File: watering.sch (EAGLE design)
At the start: 36 parts, among them IC1 LM324N, IC2 7805T, J1 DCJ0202, Q1 IRF510, T1 2N2222, T2 2N2222, T3 2N2222A

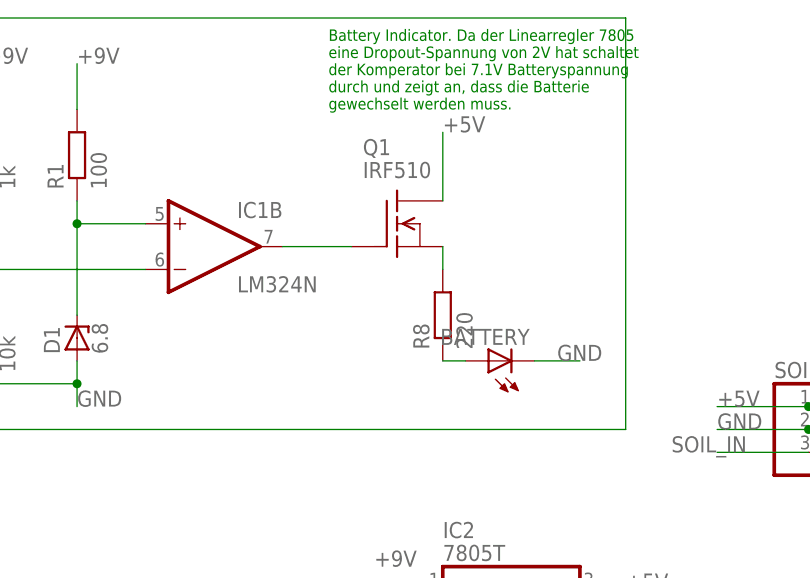
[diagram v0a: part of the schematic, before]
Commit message: Add pull-down resistor for MOSFET and changed MOSFET type to IRLZ44N
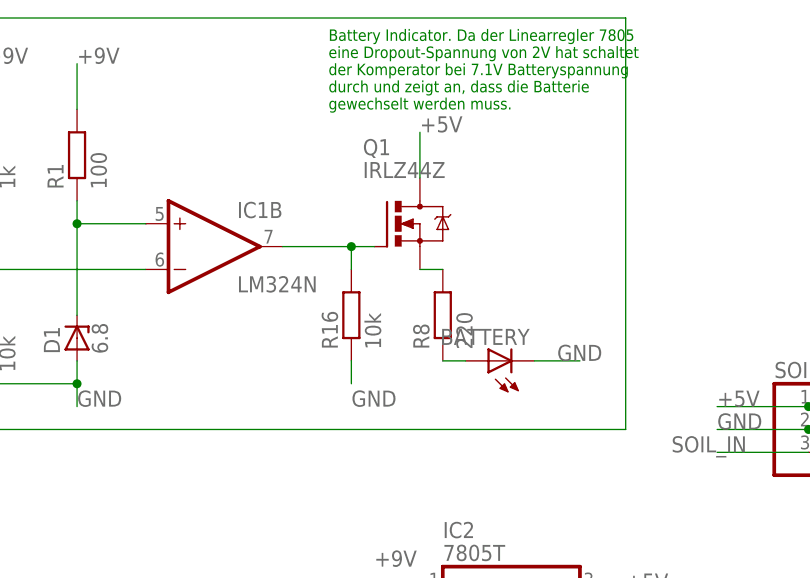
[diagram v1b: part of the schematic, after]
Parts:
- added R16: 10k, resistor:R-EU_0204/5
- Q1: value IRF510 -> IRLZ44Z; device transistor-fet:IRF510 -> transistor-power:IRLZ44Z
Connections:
- net GND: now also R16.1
- net N$7: now also R16.2
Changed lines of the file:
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@@
 <part name="R6" library="resistor" deviceset="R-EU_" device="0204/5" value="1k"/>
 <part name="R7" library="resistor" deviceset="R-EU_" device="0204/5" value="10k"/>
-<part name="Q1" library="transistor-fet" deviceset="IRF510" device=""/>
+<part name="Q1" library="transistor-power" deviceset="IRLZ44Z" device=""/>
 <part name="R8" library="resistor" deviceset="R-EU_" device="0204/5" value="220"/>
 <part name="BATTERY" library="led" deviceset="LED" device="3MM"/>
@@
 <part name="JP1" library="pinhead" deviceset="PINHD-1X1" device="" value="JP2_DSIG"/>
 <part name="R15" library="resistor" deviceset="R-EU_" device="0204/5" value="4.7k"/>
+<part name="R16" library="resistor" deviceset="R-EU_" device="0204/5" value="10k"/>
 </parts>
 <sheets>
@@
 </instance>
 <instance part="R15" gate="G$1" x="-38.1" y="-30.48" rot="R180"/>
+<instance part="R16" gate="G$1" x="-78.74" y="101.6" rot="R90"/>
 </instances>
 <busses>
@@
 <wire x1="-33.02" y1="-30.48" x2="-27.94" y2="-30.48" width="0.1524" layer="91"/>
 <label x="-30.48" y="-30.48" size="1.27" layer="95"/>
+</segment>
+<segment>
+<pinref part="R16" gate="G$1" pin="1"/>
+<wire x1="-78.74" y1="96.52" x2="-78.74" y2="93.98" width="0.1524" layer="91"/>
+<label x="-78.74" y="91.44" size="1.778" layer="95"/>
 </segment>
 </net>
@@
 <segment>
 <pinref part="Q1" gate="G$1" pin="D"/>
-<wire x1="-68.58" y1="114.3" x2="-68.58" y2="121.92" width="0.1524" layer="91"/>
-<label x="-68.58" y="121.92" size="1.778" layer="95"/>
+<wire x1="-71.12" y1="116.84" x2="-71.12" y2="121.92" width="0.1524" layer="91"/>
+<label x="-71.12" y="121.92" size="1.778" layer="95"/>
 </segment>
 <segment>
@@
 <pinref part="Q1" gate="G$1" pin="G"/>
 <wire x1="-86.36" y1="109.22" x2="-78.74" y2="109.22" width="0.1524" layer="91"/>
+<pinref part="R16" gate="G$1" pin="2"/>
+<wire x1="-78.74" y1="109.22" x2="-76.2" y2="109.22" width="0.1524" layer="91"/>
+<wire x1="-78.74" y1="106.68" x2="-78.74" y2="109.22" width="0.1524" layer="91"/>
+<junction x="-78.74" y="109.22"/>
 </segment>
 </net>
@@
 <pinref part="Q1" gate="G$1" pin="S"/>
 <pinref part="R8" gate="G$1" pin="2"/>
-<wire x1="-68.58" y1="109.22" x2="-68.58" y2="106.68" width="0.1524" layer="91"/>
-</segment>
-</net>
+<wire x1="-71.12" y1="106.68" x2="-68.58" y2="106.68" width="0.1524" layer="91"/>
+</segment>
+</net>

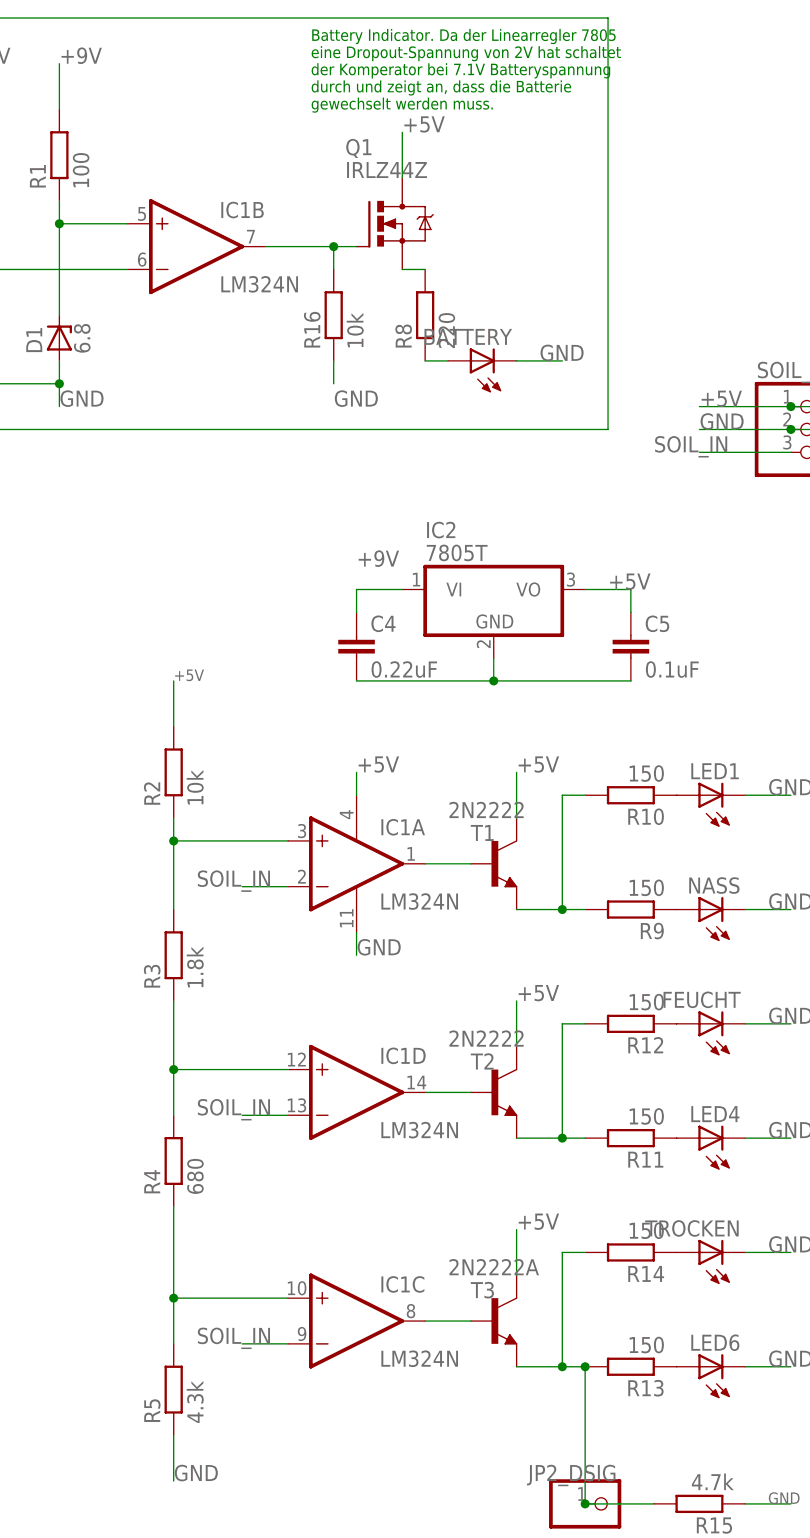
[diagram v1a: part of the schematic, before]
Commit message: Create watering indicator v2.0 for SMD
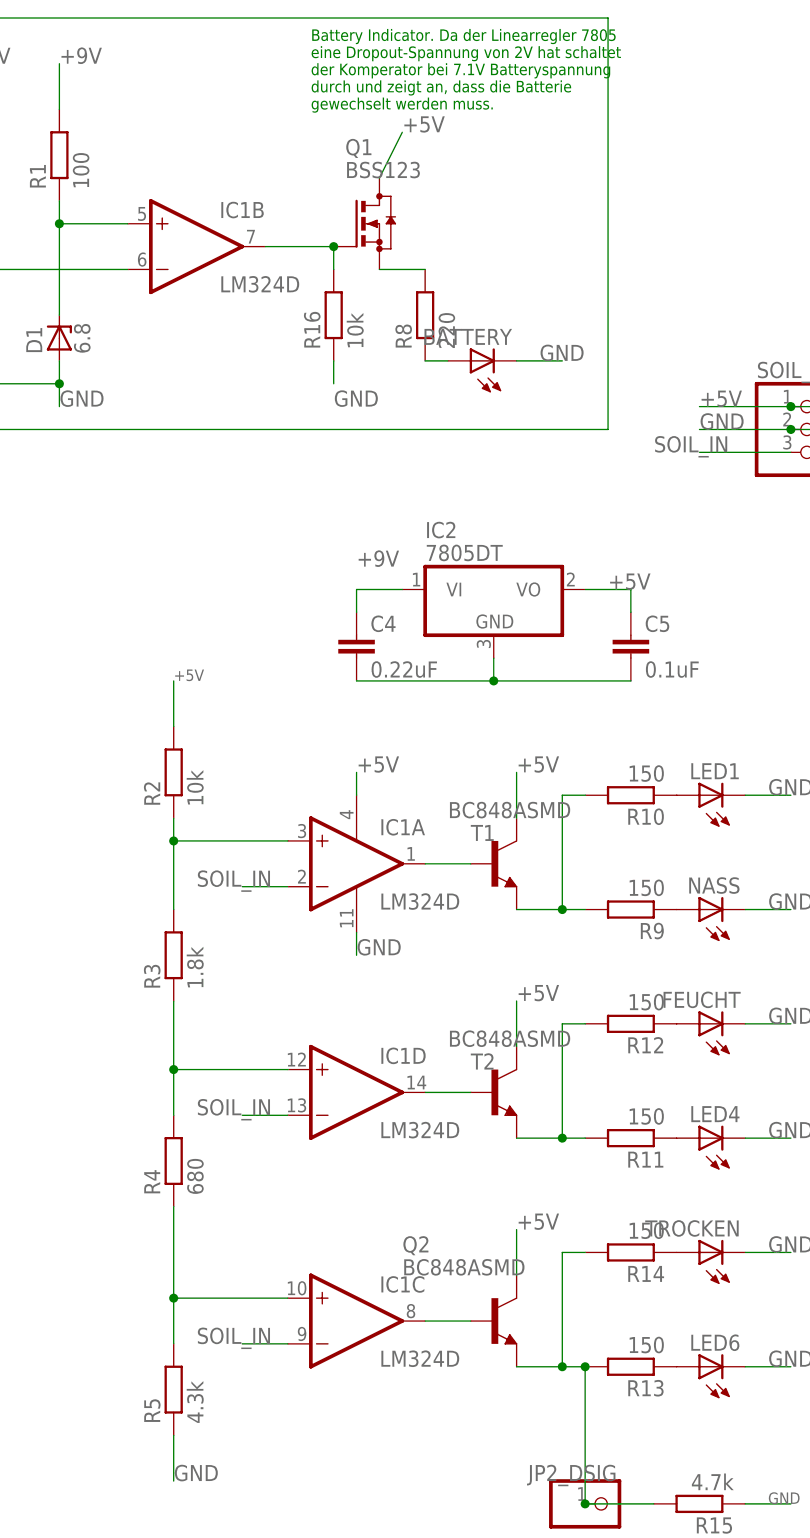
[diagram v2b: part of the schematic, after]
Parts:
- removed T3: 2N2222A, transistor-npn:2N2222A
- added Q2: BC848ASMD, transistor-npn:BC848ASMD
- BATTERY, FEUCHT, LED1, LED4, LED6, NASS, TROCKEN: device led:LED3MM -> led:LEDSML0805
- C2, C3, C4, C5: device rcl:C-EU025-025X050 -> rcl:C-EUC0805
- D1: device diode:ZENER-DIODEZD-7.5 -> diode:ZENER-DIODESOD80C
- IC1: value LM324N -> LM324D; device linear:LM324N -> linear:LM324D
- IC2: value 7805T -> 7805DT; device linear:7805T -> linear:7805DT
- Q1: value IRLZ44Z -> BSS123; device transistor-power:IRLZ44Z -> transistor-small-signal:BSS123
- R1, R10, R11, R12, R13, R14, R15, R16, R2, R3, R4, R5, R6, R7, R8, R9: device resistor:R-EU_0204/5 -> resistor:R-EU_M0805
- T1, T2: value 2N2222 -> BC848ASMD; device transistor:2N2222 -> transistor-npn:BC848ASMD
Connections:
- net +5V: now also Q2.C; no longer T3.C
- net N$18: now also Q2.E; no longer T3.E
- net N$5: now also Q2.B; no longer T3.B

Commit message: Update smd version
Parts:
- removed C2: 0.1uF, rcl:C-EUC0805
- removed IC2: 7805DT, linear:7805DT
- removed SOIL_MOIST: (no value), pinhead:PINHD-1X3
- added C1: 0.1uF, rcl:C-EUC0805
- added R17, R18: 4.7k, resistor:R-EU_M0805
- added REG1: 7805DT, linear:7805DT
- JP1: device pinhead:PINHD-1X1 -> jumper:JP3Q
- renumbered Q1 to MOS1, Q2 to T3
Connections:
- removed net N$14: R10.2, R9.2, T1.E
- removed net N$15: R11.2, R12.2, T2.E
- removed net N$18: JP1.1, R13.2, R14.2, R15.2, T3.E
- new net FEUCHT: JP1.3, R11.2, R12.2, R17.2, T2.E
- new net NASS: JP1.1, R10.2, R18.2, R9.2, T1.E
- new net TROCKEN: JP1.5, R13.2, R14.2, R15.2, T3.E
- net +5V: now also C1.2, IC1A.+IN, JP1.4, REG1.VO; no longer C2.1, IC2.VO, SOIL_MOIST.1
- net +9V: now also REG1.VI; no longer IC2.VI
- net GND: now also C1.1, JP1.6, R17.1, R18.1, REG1.GND; no longer C2.2, IC2.GND, SOIL_MOIST.2
- net N$1: no longer IC1A.+IN
- net SOIL_IN: now also JP1.2; no longer SOIL_MOIST.3
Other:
- moved on the sheet: C4, C5, R15

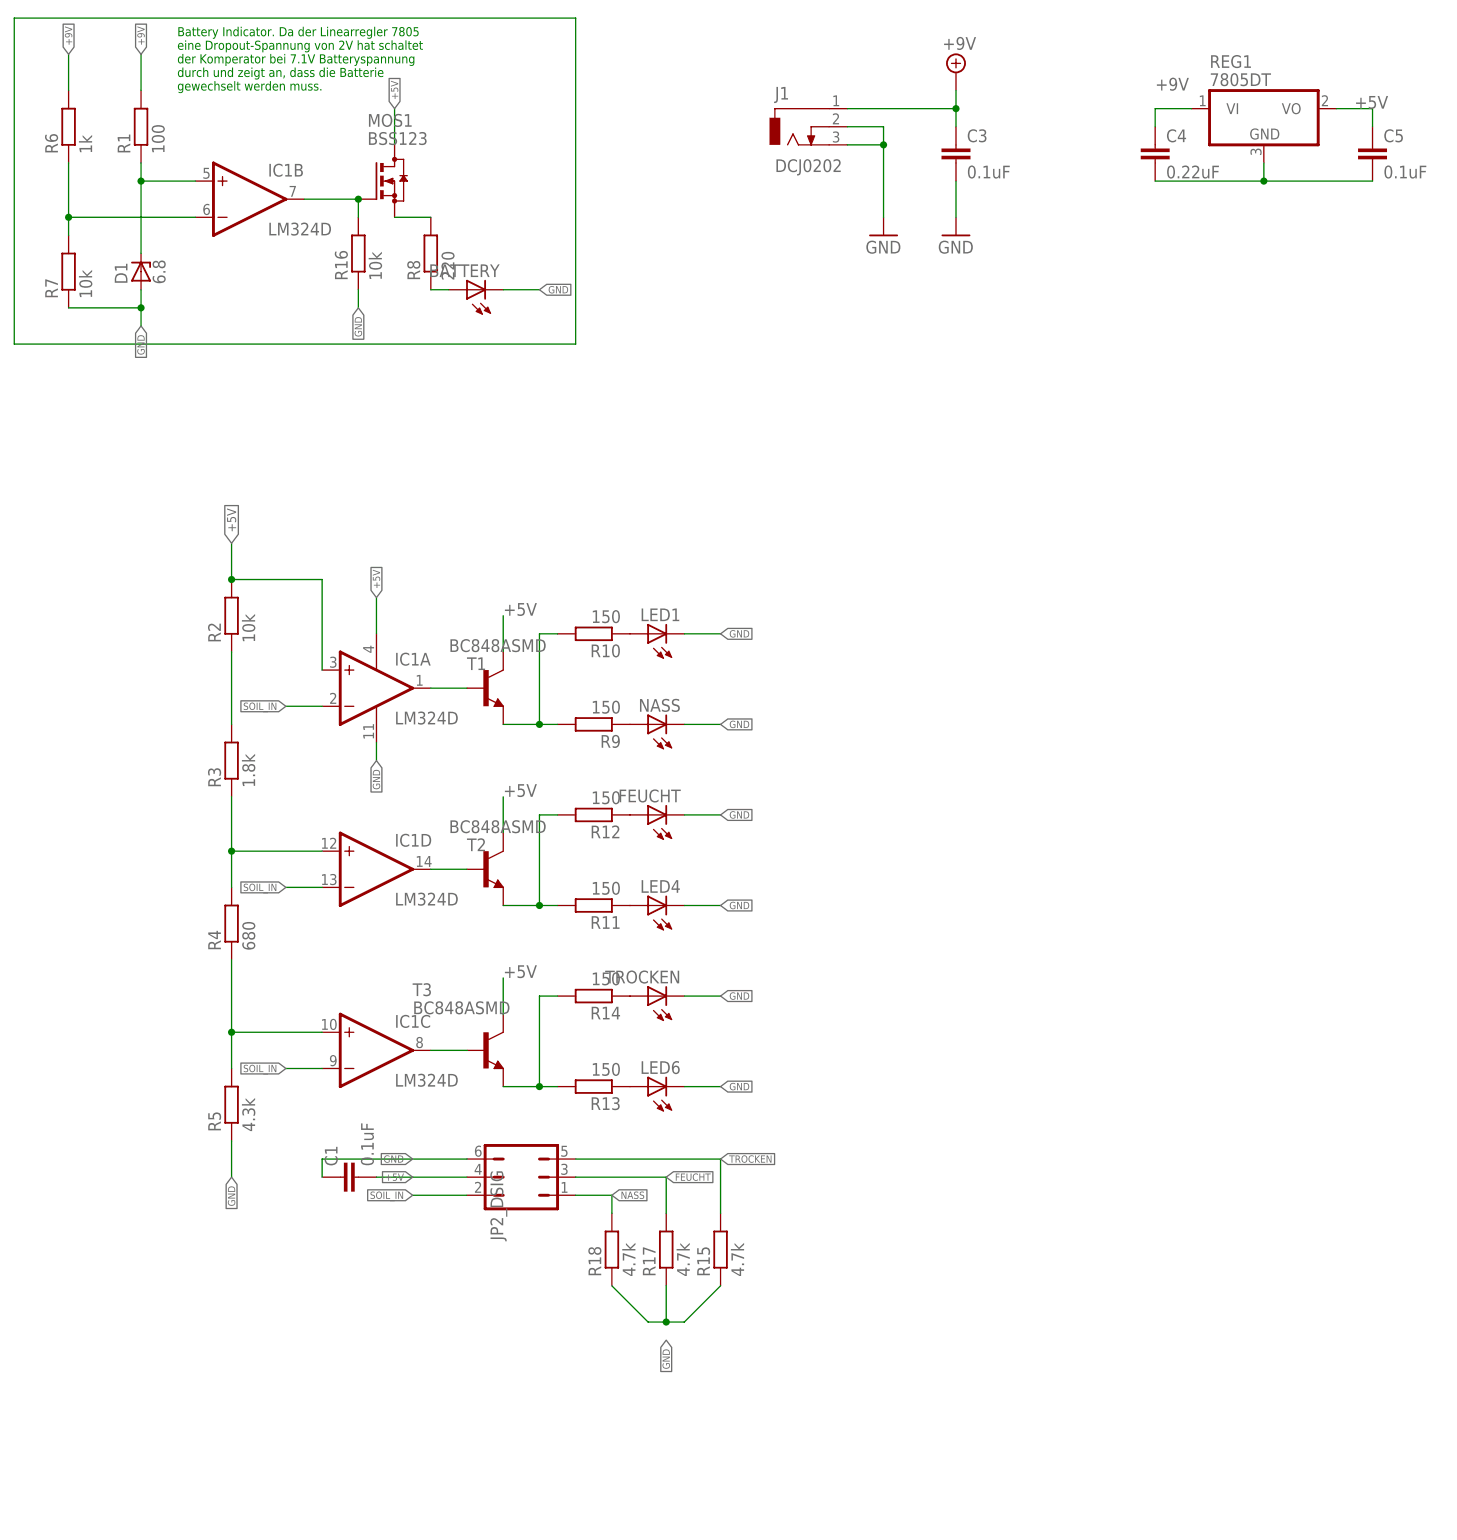
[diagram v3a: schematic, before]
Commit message: Replace BJT to MOSFET for led switching
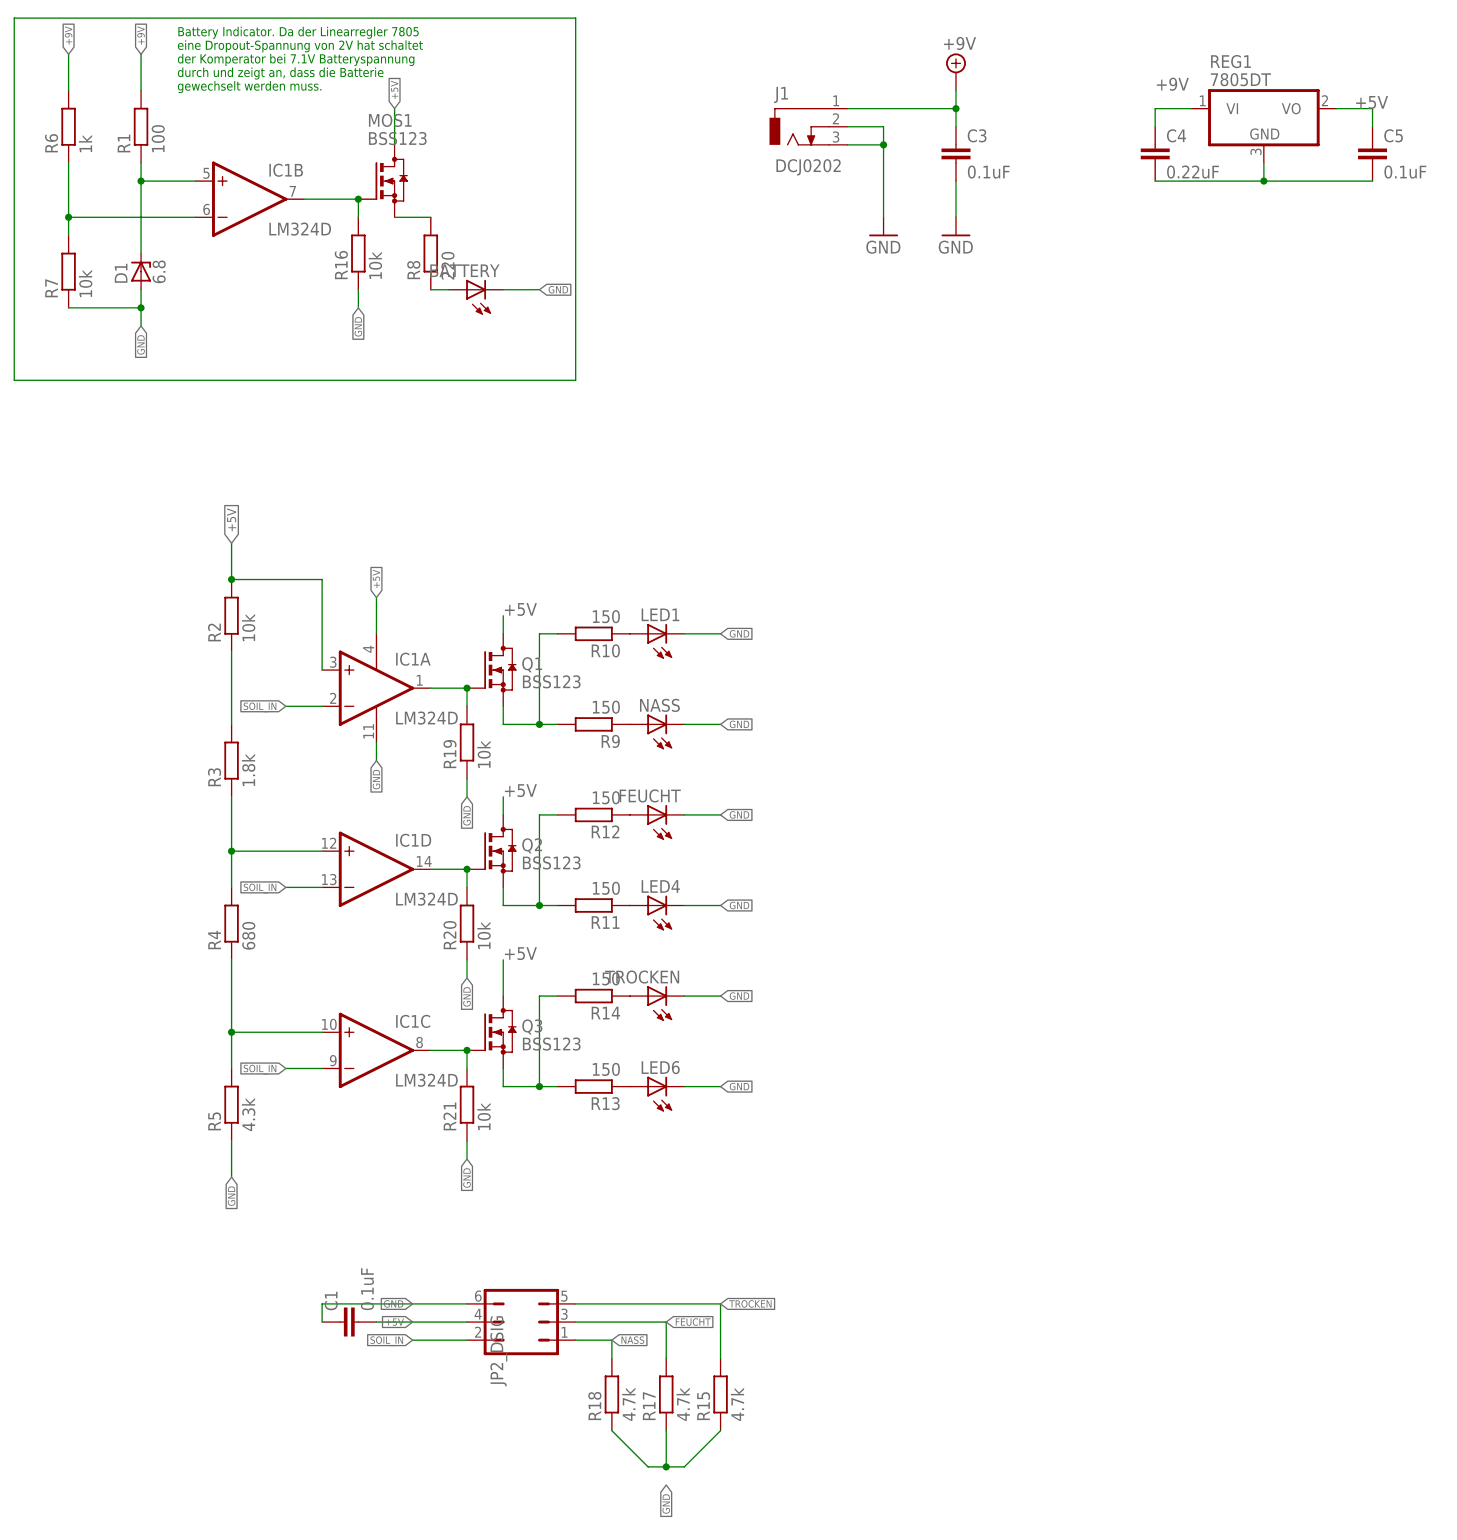
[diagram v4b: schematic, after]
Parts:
- removed T1, T2, T3: BC848ASMD, transistor-npn:BC848ASMD
- added Q1, Q2, Q3: BSS123, transistor-small-signal:BSS123
- added R19, R20, R21: 10k, resistor:R-EU_M0805
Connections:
- net +5V: now also Q1.D, Q2.D, Q3.D; no longer T1.C, T2.C, T3.C
- net FEUCHT: now also Q2.S; no longer T2.E
- net GND: now also R19.1, R20.1, R21.1
- net N$2: now also Q1.G, R19.2; no longer T1.B
- net N$4: now also Q2.G, R20.2; no longer T2.B
- net N$5: now also Q3.G, R21.2; no longer T3.B
- net NASS: now also Q1.S; no longer T1.E
- net TROCKEN: now also Q3.S; no longer T3.E
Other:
- moved on the sheet: C1, R15, R17, R18
